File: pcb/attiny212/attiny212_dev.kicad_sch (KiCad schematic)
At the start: 9 parts, among them J1 USB_B_Micro, U1 CH340C, U2 ATtiny212-SS

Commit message: create
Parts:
- removed C2: 10u, symbol Device:C
- removed C3, C4: 0.1u, symbol Device:C
- removed D1: D, symbol Device:D
- removed J1: USB_B_Micro, symbol Connector:USB_B_Micro
- removed U1: CH340C, Package_SO:SOIC-16_3.9x9.9mm_P1.27mm, symbol Interface_USB:CH340C
- added D1: LED, LED_THT:LED_D3.0mm, symbol Device:LED
- added J1, J3, J4, J5: Conn_01x06, Connector_PinHeader_2.54mm:PinHeader_1x06_P2.54mm_Vertical, symbol Connector_Generic:Conn_01x06
- added J2: Conn_01x03, Connector_PinHeader_2.54mm:PinHeader_1x03_P2.54mm_Vertical, symbol Connector_Generic:Conn_01x03
- added JP1, JP2: Jumper_2_Bridged, Connector_PinHeader_2.54mm:PinHeader_1x02_P2.54mm_Vertical, symbol Jumper:Jumper_2_Bridged
- C1: footprint (none) -> Capacitor_SMD:C_1210_3225Metric_Pad1.33x2.70mm_HandSolder
- R1: value 470 -> 330; footprint (none) -> Resistor_THT:R_Axial_DIN0207_L6.3mm_D2.5mm_P10.16mm_Horizontal
- renumbered U2 to U1
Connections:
- net +5V: now also J2.1 (Pin_1), J3.1 (Pin_1), J3.2 (Pin_2), J3.3 (Pin_3), J3.4 (Pin_4), J3.5 (Pin_5), J3.6 (Pin_6), JP1.1 (A)
- net GND: now also R1.2, J1.6 (Pin_6), J2.3 (Pin_3), J5.1 (Pin_1), J5.2 (Pin_2), J5.3 (Pin_3), J5.4 (Pin_4), J5.5 (Pin_5), J5.6 (Pin_6)
- net RxD: now also J1.3 (Pin_3), J4.6 (Pin_6)
- net TxD: now also J1.2 (Pin_2), J4.5 (Pin_5)
- net UPDI: now also J2.2 (Pin_2), J4.1 (Pin_1)
- net at R1.1: now also D1.1 (K)
- net PA1: now reaches U1.4 (PA1)
- net PA1: now also J4.2 (Pin_2), JP2.1 (A)
- net PA2: now reaches U1.5 (PA2)
- net PA2: now also J4.3 (Pin_3)
- net PA3: now reaches U1.7 (PA3)
- net PA3: now also J4.4 (Pin_4)
- new net: J1.4 (Pin_4), JP1.2 (B)
- new net: D1.2 (A), JP2.2 (B)
- no-connect marks 9 -> 2
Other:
- moved on the sheet: C1, U1

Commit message: resurect
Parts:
- added C2, C4: 100nF, symbol Device:C
- added C3: 10uF, symbol Device:C
- added D2: PMEG6020ER, Diode_SMD:Nexperia_CFP3_SOD-123W, symbol Diode:PMEG6020ER
- added J6: USB_B_Micro, symbol Connector:USB_B_Micro
- added U2: CH340C, Package_SO:SOIC-16_3.9x9.9mm_P1.27mm, symbol Interface_USB:CH340C
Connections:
- net GND: now also C2.2, C3.2, C4.2, J6.5 (GND), J6.6 (Shield), U2.1 (GND)
- new net: C2.1, U2.4 (V3)
- new net: J6.3 (D+), U2.5 (UD+)
- new net: J6.2 (D-), U2.6 (UD-)
- new net VBUS: D2.2 (A), J6.1 (VBUS)
- new net VSYS: C3.1, C4.1, D2.1 (K), U2.16 (VCC)
- no-connect marks 2 -> 10
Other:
- moved on the sheet: J2

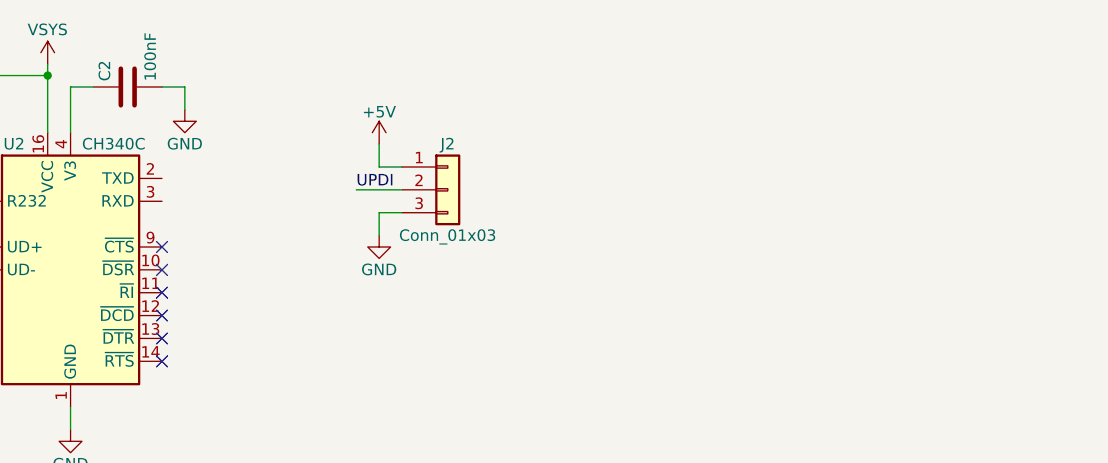
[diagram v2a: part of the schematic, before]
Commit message: Update attiny212_dev.kicad_sch
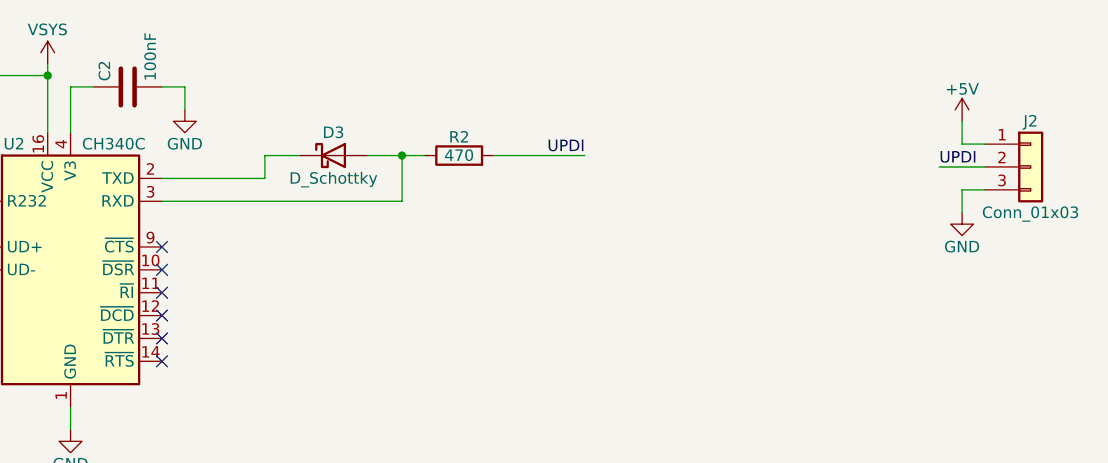
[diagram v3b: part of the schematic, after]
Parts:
- added D3: D_Schottky, symbol Device:D_Schottky
- added R2: 470, symbol Device:R
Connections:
- net UPDI: now also R2.2
- net at U2.2 (TXD): now also D3.1 (K)
- net at U2.3 (RXD): now also D3.2 (A), R2.1
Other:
- moved on the sheet: J2
